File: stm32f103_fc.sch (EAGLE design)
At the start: 46 parts, among them IC1 STM32F10XCXT6, IC2 LD117AS33TR, J5 1X2-3.5MM, J6 1X2-3.5MM, U2 9DoF IMU, Y1 8MHz, Y2 32.768MHz

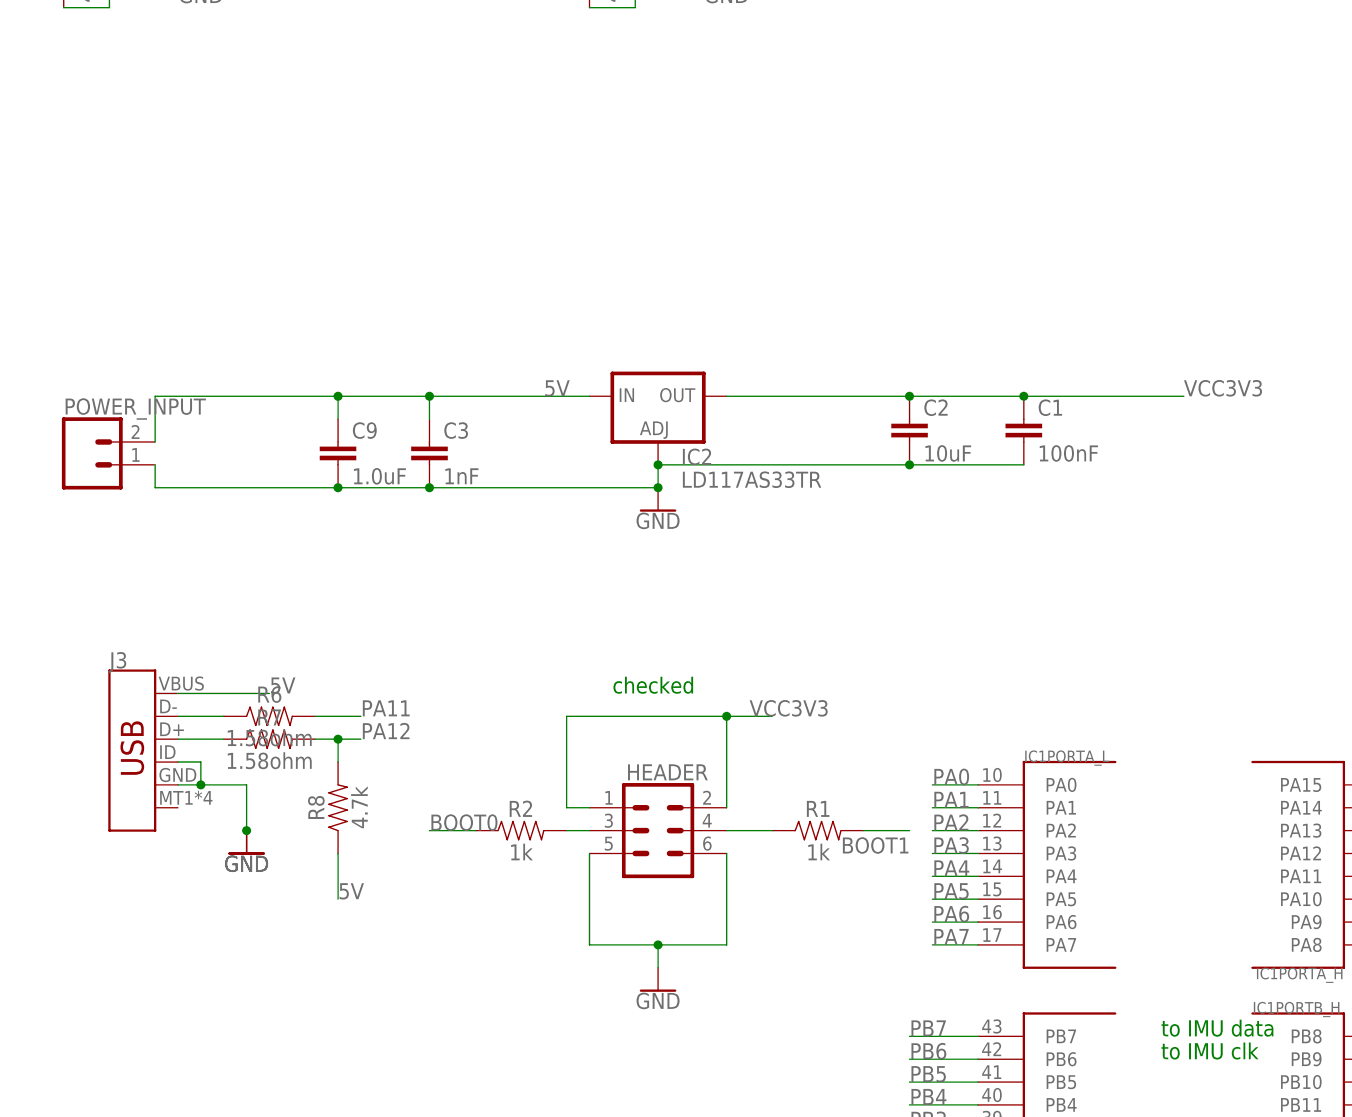
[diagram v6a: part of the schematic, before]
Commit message: added servo controller
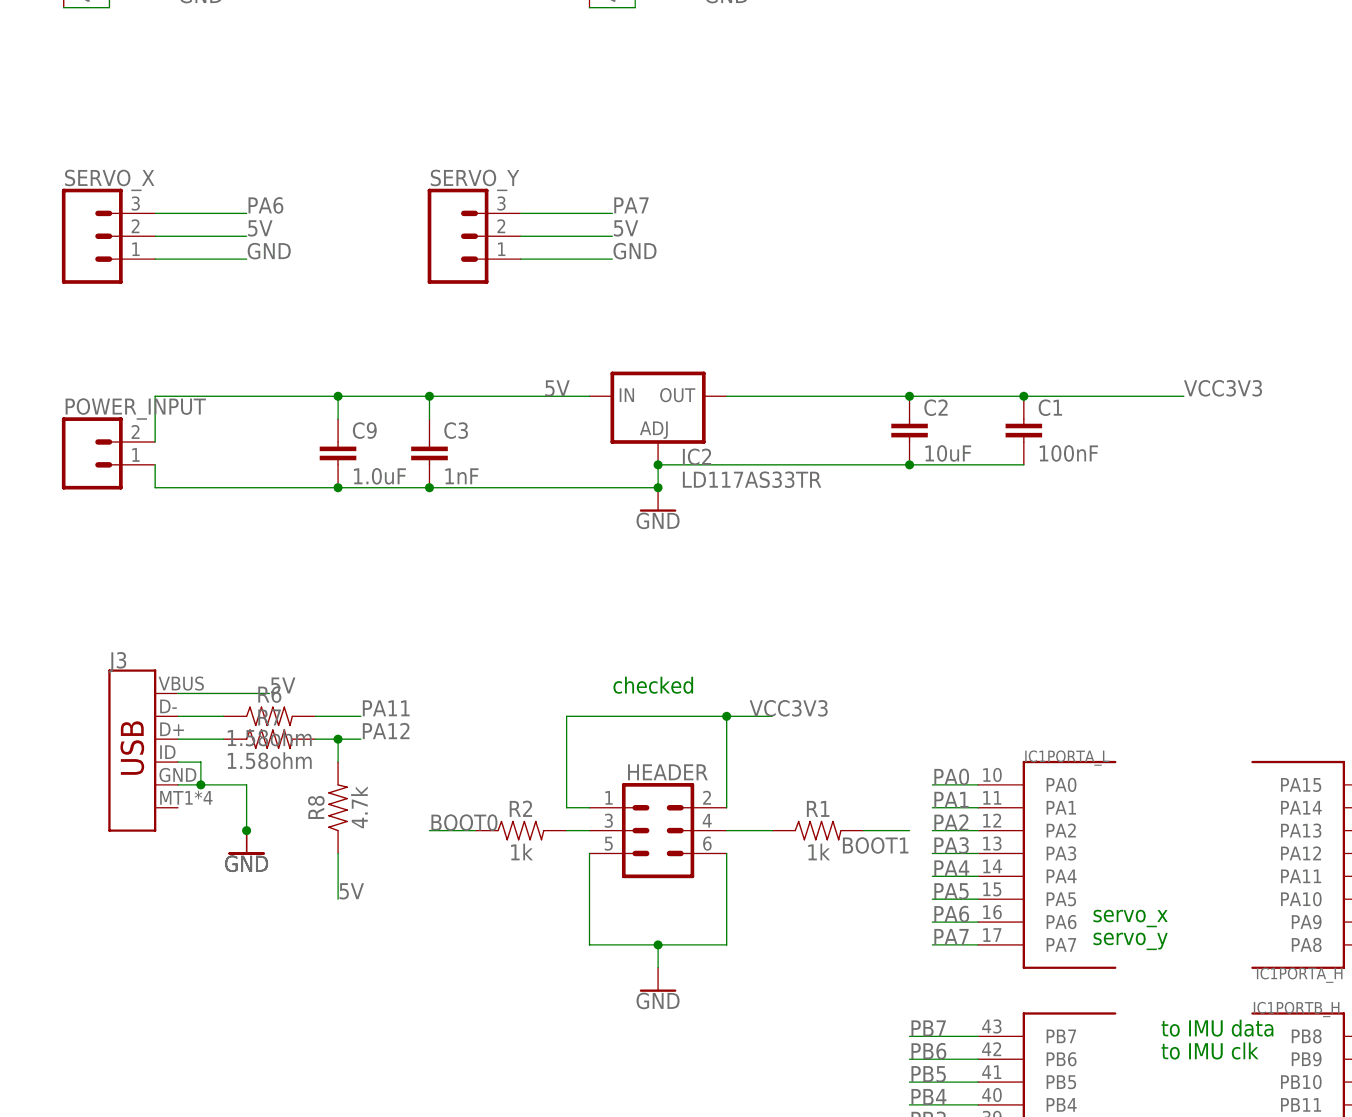
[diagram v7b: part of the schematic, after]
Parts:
- added SERVO_X, SERVO_Y: (no value), SparkFun-Connectors:CONN_03
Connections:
- net 5V: now also SERVO_X.2, SERVO_Y.2
- net GND: now also SERVO_X.1, SERVO_Y.1
- net PA6: now also SERVO_X.3
- net PA7: now also SERVO_Y.3
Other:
- note added: "servo_x"
- note added: "servo_y"
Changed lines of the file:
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@@
 <part name="S1" library="SparkFun-Switches" library_urn="urn:adsk.eagle:library:535" deviceset="MOMENTARY-SWITCH-SPST" device="-SMD-5.2-REDUNDANT" package3d_urn="urn:adsk.eagle:package:40167/1" value="SPST-SMD-5.2"/>
 <part name="GND2" library="SparkFun-PowerSymbols" library_urn="urn:adsk.eagle:library:530" deviceset="GND" device=""/>
+<part name="SERVO_X" library="SparkFun-Connectors" library_urn="urn:adsk.eagle:library:513" deviceset="CONN_03" device="" package3d_urn="urn:adsk.eagle:package:38063/1"/>
+<part name="SERVO_Y" library="SparkFun-Connectors" library_urn="urn:adsk.eagle:library:513" deviceset="CONN_03" device="" package3d_urn="urn:adsk.eagle:package:38063/1"/>
 </parts>
 <sheets>
@@
 <text x="193.04" y="73.66" size="1.778" layer="91">checked</text>
 <text x="132.08" y="38.1" size="1.778" layer="91">checked</text>
+<text x="48.26" y="68.58" size="1.778" layer="91">servo_x</text>
+<text x="48.26" y="66.04" size="1.778" layer="91">servo_y</text>
 </plain>
 <instances>
@@
 <instance part="GND2" gate="1" x="200.66" y="15.24" smashed="yes" rot="R90">
 <attribute name="VALUE" x="200.914" y="15.24" size="1.778" layer="96" rot="R90" align="top-center"/>
+</instance>
+<instance part="SERVO_X" gate="J$1" x="-63.5" y="144.78" smashed="yes">
+<attribute name="VALUE" x="-66.04" y="137.414" size="1.778" layer="96" font="vector"/>
+<attribute name="NAME" x="-66.04" y="150.368" size="1.778" layer="95" font="vector"/>
+</instance>
+<instance part="SERVO_Y" gate="J$1" x="-22.86" y="144.78" smashed="yes">
+<attribute name="VALUE" x="-25.4" y="137.414" size="1.778" layer="96" font="vector"/>
+<attribute name="NAME" x="-25.4" y="150.368" size="1.778" layer="95" font="vector"/>
 </instance>
 </instances>
@@
 <junction x="0" y="116.84"/>
 </segment>
+<segment>
+<pinref part="SERVO_X" gate="J$1" pin="1"/>
+<wire x1="-55.88" y1="142.24" x2="-45.72" y2="142.24" width="0.1524" layer="91"/>
+<label x="-45.72" y="142.24" size="1.778" layer="95"/>
+</segment>
+<segment>
+<pinref part="SERVO_Y" gate="J$1" pin="1"/>
+<wire x1="-15.24" y1="142.24" x2="-5.08" y2="142.24" width="0.1524" layer="91"/>
+<label x="-5.08" y="142.24" size="1.778" layer="95"/>
+</segment>
 </net>
 <net name="5V" class="0">
@@
 <label x="7.62" y="193.04" size="1.778" layer="95"/>
 </segment>
+<segment>
+<pinref part="SERVO_X" gate="J$1" pin="2"/>
+<wire x1="-55.88" y1="144.78" x2="-45.72" y2="144.78" width="0.1524" layer="91"/>
+<label x="-45.72" y="144.78" size="1.778" layer="95"/>
+</segment>
+<segment>
+<pinref part="SERVO_Y" gate="J$1" pin="2"/>
+<wire x1="-15.24" y1="144.78" x2="-5.08" y2="144.78" width="0.1524" layer="91"/>
+<label x="-5.08" y="144.78" size="1.778" layer="95"/>
+</segment>
 </net>
 <net name="N$3" class="0">
@@
 <pinref part="IC1" gate="PORTA_L" pin="PA6"/>
 </segment>
+<segment>
+<pinref part="SERVO_X" gate="J$1" pin="3"/>
+<wire x1="-55.88" y1="147.32" x2="-45.72" y2="147.32" width="0.1524" layer="91"/>
+<label x="-45.72" y="147.32" size="1.778" layer="95"/>
+</segment>
 </net>
 <net name="PA7" class="0">
@@
 <pinref part="IC1" gate="PORTA_L" pin="PA7"/>
 </segment>
-</net>
+<segment>
+<pinref part="SERVO_Y" gate="J$1" pin="3"/>
+<wire x1="-15.24" y1="147.32" x2="-5.08" y2="147.32" width="0.1524" layer="91"/>
+<label x="-5.08" y="147.32" size="1.778" layer="95"/>
+</segment>
+</net>

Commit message: BOM next
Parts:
- Q1, Q2: device adafruit:MOSFET-NGDS_TO220V -> adafruit:MOSFET-NREFLOW
- renumbered J5 to PYRO2, J6 to PYRO1
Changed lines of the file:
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@@
 <grid distance="0.1" unitdist="inch" unit="inch" style="lines" multiple="1" display="no" altdistance="0.01" altunitdist="inch" altunit="inch"/>
 <layers>
-<layer number="1" name="Top" color="4" fill="1" visible="no" active="no"/>
-<layer number="16" name="Bottom" color="1" fill="1" visible="no" active="no"/>
-<layer number="17" name="Pads" color="2" fill="1" visible="no" active="no"/>
-<layer number="18" name="Vias" color="2" fill="1" visible="no" active="no"/>
-<layer number="19" name="Unrouted" color="6" fill="1" visible="no" active="no"/>
-<layer number="20" name="Dimension" color="15" fill="1" visible="no" active="no"/>
-<layer number="21" name="tPlace" color="7" fill="1" visible="no" active="no"/>
-<layer number="22" name="bPlace" color="7" fill="1" visible="no" active="no"/>
-<layer number="23" name="tOrigins" color="15" fill="1" visible="no" active="no"/>
-<layer number="24" name="bOrigins" color="15" fill="1" visible="no" active="no"/>
-<layer number="25" name="tNames" color="7" fill="1" visible="no" active="no"/>
-<layer number="26" name="bNames" color="7" fill="1" visible="no" active="no"/>
-<layer number="27" name="tValues" color="7" fill="1" visible="no" active="no"/>
-<layer number="28" name="bValues" color="7" fill="1" visible="no" active="no"/>
+<layer number="1" name="Top" color="4" fill="1" visible="yes" active="no"/>
+<layer number="16" name="Bottom" color="1" fill="1" visible="yes" active="no"/>
+<layer number="17" name="Pads" color="2" fill="1" visible="yes" active="no"/>
+<layer number="18" name="Vias" color="2" fill="1" visible="yes" active="no"/>
+<layer number="19" name="Unrouted" color="6" fill="1" visible="yes" active="no"/>
+<layer number="20" name="Dimension" color="24" fill="1" visible="yes" active="no"/>
+<layer number="21" name="tPlace" color="7" fill="1" visible="yes" active="no"/>
+<layer number="22" name="bPlace" color="7" fill="1" visible="yes" active="no"/>
+<layer number="23" name="tOrigins" color="15" fill="1" visible="yes" active="no"/>
+<layer number="24" name="bOrigins" color="15" fill="1" visible="yes" active="no"/>
+<layer number="25" name="tNames" color="7" fill="1" visible="yes" active="no"/>
+<layer number="26" name="bNames" color="7" fill="1" visible="yes" active="no"/>
+<layer number="27" name="tValues" color="7" fill="1" visible="yes" active="no"/>
+<layer number="28" name="bValues" color="7" fill="1" visible="yes" active="no"/>
 <layer number="29" name="tStop" color="7" fill="3" visible="no" active="no"/>
 <layer number="30" name="bStop" color="7" fill="6" visible="no" active="no"/>
@@
 <layer number="35" name="tGlue" color="7" fill="4" visible="no" active="no"/>
 <layer number="36" name="bGlue" color="7" fill="5" visible="no" active="no"/>
-<layer number="37" name="tTest" color="7" fill="1" visible="no" active="no"/>
-<layer number="38" name="bTest" color="7" fill="1" visible="no" active="no"/>
+<layer number="37" name="tTest" color="7" fill="1" visible="yes" active="no"/>
+<layer number="38" name="bTest" color="7" fill="1" visible="yes" active="no"/>
 <layer number="39" name="tKeepout" color="4" fill="11" visible="no" active="no"/>
 <layer number="40" name="bKeepout" color="1" fill="11" visible="no" active="no"/>
@@
 <layer number="44" name="Drills" color="7" fill="1" visible="no" active="no"/>
 <layer number="45" name="Holes" color="7" fill="1" visible="no" active="no"/>
-<layer number="46" name="Milling" color="3" fill="1" visible="no" active="no"/>
-<layer number="47" name="Measures" color="7" fill="1" visible="no" active="no"/>
-<layer number="48" name="Document" color="7" fill="1" visible="no" active="no"/>
-<layer number="49" name="Reference" color="7" fill="1" visible="no" active="no"/>
-<layer number="50" name="dxf" color="7" fill="1" visible="no" active="no"/>
-<layer number="51" name="tDocu" color="7" fill="1" visible="no" active="no"/>
-<layer number="52" name="bDocu" color="7" fill="1" visible="no" active="no"/>
-<layer number="53" name="tGND_GNDA" color="7" fill="9" visible="no" active="no"/>
-<layer number="54" name="bGND_GNDA" color="1" fill="9" visible="no" active="no"/>
-<layer number="56" name="wert" color="7" fill="1" visible="no" active="no"/>
-<layer number="57" name="tCAD" color="7" fill="1" visible="no" active="no"/>
-<layer number="59" name="tCarbon" color="7" fill="1" visible="no" active="no"/>
-<layer number="60" name="bCarbon" color="7" fill="1" visible="no" active="no"/>
+<layer number="46" name="Milling" color="3" fill="1" visible="yes" active="no"/>
+<layer number="47" name="Measures" color="7" fill="1" visible="yes" active="no"/>
+<layer number="48" name="Document" color="7" fill="1" visible="yes" active="no"/>
+<layer number="49" name="Reference" color="7" fill="1" visible="yes" active="no"/>
+<layer number="50" name="dxf" color="7" fill="1" visible="yes" active="no"/>
+<layer number="51" name="tDocu" color="7" fill="1" visible="yes" active="no"/>
+<layer number="52" name="bDocu" color="7" fill="1" visible="yes" active="no"/>
+<layer number="53" name="tGND_GNDA" color="7" fill="9" visible="yes" active="no"/>
+<layer number="54" name="bGND_GNDA" color="1" fill="9" visible="yes" active="no"/>
+<layer number="56" name="wert" color="7" fill="1" visible="yes" active="no"/>
+<layer number="57" name="tCAD" color="7" fill="1" visible="yes" active="no"/>
+<layer number="59" name="tCarbon" color="7" fill="1" visible="yes" active="no"/>
+<layer number="60" name="bCarbon" color="7" fill="1" visible="yes" active="no"/>
 <layer number="88" name="SimResults" color="9" fill="1" visible="yes" active="yes"/>
 <layer number="89" name="SimProbes" color="9" fill="1" visible="yes" active="yes"/>
@@
 <part name="GND28" library="SparkFun-PowerSymbols" library_urn="urn:adsk.eagle:library:530" deviceset="GND" device=""/>
 <part name="POWER_INPUT" library="SparkFun-Connectors" library_urn="urn:adsk.eagle:library:513" deviceset="CONN_02" device="3.5MM" package3d_urn="urn:adsk.eagle:package:38050/1"/>
-<part name="J6" library="adafruit" library_urn="urn:adsk.eagle:library:420" deviceset="1X2" device="-3.5MM" package3d_urn="urn:adsk.eagle:package:6240635/1"/>
-<part name="Q1" library="adafruit" library_urn="urn:adsk.eagle:library:420" deviceset="MOSFET-N" device="GDS_TO220V" package3d_urn="urn:adsk.eagle:package:6240882/1"/>
+<part name="PYRO1" library="adafruit" library_urn="urn:adsk.eagle:library:420" deviceset="1X2" device="-3.5MM" package3d_urn="urn:adsk.eagle:package:6240635/1"/>
+<part name="Q1" library="adafruit" library_urn="urn:adsk.eagle:library:420" deviceset="MOSFET-N" device="REFLOW" package3d_urn="urn:adsk.eagle:package:6240836/1"/>
 <part name="GND31" library="SparkFun-PowerSymbols" library_urn="urn:adsk.eagle:library:530" deviceset="GND" device=""/>
-<part name="J5" library="adafruit" library_urn="urn:adsk.eagle:library:420" deviceset="1X2" device="-3.5MM" package3d_urn="urn:adsk.eagle:package:6240635/1"/>
-<part name="Q2" library="adafruit" library_urn="urn:adsk.eagle:library:420" deviceset="MOSFET-N" device="GDS_TO220V" package3d_urn="urn:adsk.eagle:package:6240882/1"/>
+<part name="PYRO2" library="adafruit" library_urn="urn:adsk.eagle:library:420" deviceset="1X2" device="-3.5MM" package3d_urn="urn:adsk.eagle:package:6240635/1"/>
+<part name="Q2" library="adafruit" library_urn="urn:adsk.eagle:library:420" deviceset="MOSFET-N" device="REFLOW" package3d_urn="urn:adsk.eagle:package:6240836/1"/>
 <part name="GND30" library="SparkFun-PowerSymbols" library_urn="urn:adsk.eagle:library:530" deviceset="GND" device=""/>
 <part name="R14" library="SparkFun-Resistors" library_urn="urn:adsk.eagle:library:532" deviceset="1KOHM" device="-0603-1/10W-1%" package3d_urn="urn:adsk.eagle:package:39650/1" value="470ohm"/>
@@
 <attribute name="NAME" x="-66.04" y="124.968" size="1.778" layer="95" font="vector"/>
 </instance>
-<instance part="J6" gate="G$1" x="-25.4" y="190.5" smashed="yes"/>
+<instance part="PYRO1" gate="G$1" x="-25.4" y="190.5" smashed="yes"/>
 <instance part="Q1" gate="G$1" x="-53.34" y="182.88" smashed="yes">
 <attribute name="NAME" x="-48.26" y="183.515" size="1.27" layer="95"/>
@@
 <attribute name="VALUE" x="-50.8" y="172.466" size="1.778" layer="96" align="top-center"/>
 </instance>
-<instance part="J5" gate="G$1" x="33.02" y="190.5" smashed="yes"/>
+<instance part="PYRO2" gate="G$1" x="33.02" y="190.5" smashed="yes"/>
 <instance part="Q2" gate="G$1" x="5.08" y="182.88" smashed="yes">
 <attribute name="NAME" x="10.16" y="183.515" size="1.27" layer="95"/>
@@
 </segment>
 <segment>
-<pinref part="J6" gate="G$1" pin="1"/>
+<pinref part="PYRO1" gate="G$1" pin="1"/>
 <wire x1="-30.48" y1="193.04" x2="-50.8" y2="193.04" width="0.1524" layer="91"/>
 <label x="-50.8" y="193.04" size="1.778" layer="95"/>
 </segment>
 <segment>
-<pinref part="J5" gate="G$1" pin="1"/>
+<pinref part="PYRO2" gate="G$1" pin="1"/>
 <wire x1="27.94" y1="193.04" x2="7.62" y2="193.04" width="0.1524" layer="91"/>
 <label x="7.62" y="193.04" size="1.778" layer="95"/>
@@
 <net name="N$14" class="0">
 <segment>
-<pinref part="J6" gate="G$1" pin="2"/>
+<pinref part="PYRO1" gate="G$1" pin="2"/>
 <wire x1="-30.48" y1="190.5" x2="-35.56" y2="190.5" width="0.1524" layer="91"/>
 <pinref part="R10" gate="G$1" pin="1"/>
@@
 <net name="N$12" class="0">
 <segment>
-<pinref part="J5" gate="G$1" pin="2"/>
+<pinref part="PYRO2" gate="G$1" pin="2"/>
 <wire x1="27.94" y1="190.5" x2="22.86" y2="190.5" width="0.1524" layer="91"/>
 <pinref part="R13" gate="G$1" pin="1"/>
